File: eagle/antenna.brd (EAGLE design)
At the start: 120.7 x 57.1 mm, 23 parts

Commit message: cleaner antenna layout
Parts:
- C15: value 68 -> 86
- Q1: value (none) -> BUF730F
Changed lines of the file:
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@@
 </autorouter>
 <elements>
-<element name="Q1" library="transistor-small-signal" library_urn="urn:adsk.eagle:library:401" package="SOT343R" value="" x="14.605" y="29.21" smashed="yes" rot="R90">
-<attribute name="VALUE" x="17.305" y="28.11" size="1.27" layer="27" rot="R90"/>
-</element>
+<element name="Q1" library="transistor-small-signal" library_urn="urn:adsk.eagle:library:401" package="SOT343R" value="BUF730F" x="14.605" y="29.21" smashed="yes" rot="R90"/>
 <element name="L3" library="ref-packages-longpad" library_urn="urn:adsk.eagle:library:337" package="R0402" value="" x="12.065" y="30.48" smashed="yes" rot="R90">
 <attribute name="VALUE" x="13.97" y="29.845" size="1.27" layer="27" rot="R90"/>
@@
 <attribute name="VALUE" x="2.54" y="40.605" size="0.0254" layer="27"/>
 </element>
-<element name="C15" library="ref-packages-longpad" library_urn="urn:adsk.eagle:library:337" package="R0402" value="68" x="17.78" y="27.305" smashed="yes" rot="R180"/>
+<element name="C15" library="ref-packages-longpad" library_urn="urn:adsk.eagle:library:337" package="R0402" value="86" x="17.78" y="27.305" smashed="yes" rot="R180"/>
 </elements>
 <signals>

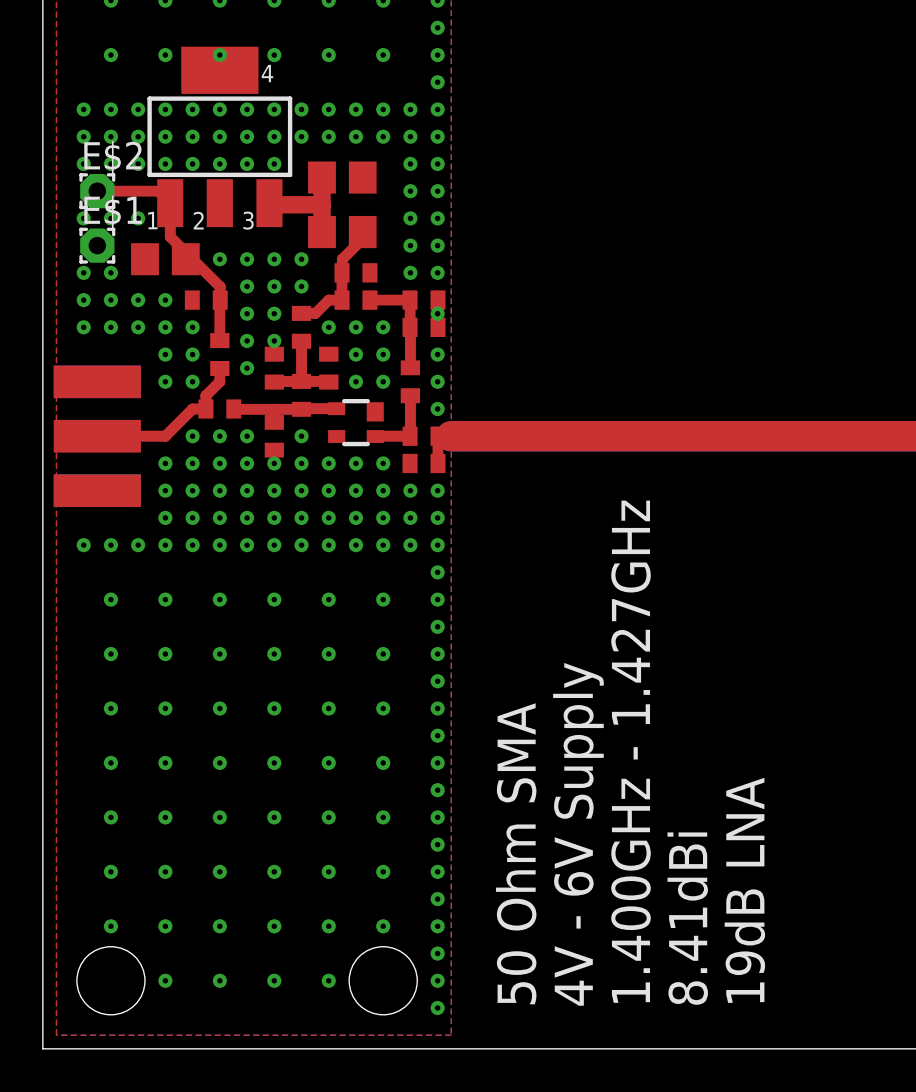
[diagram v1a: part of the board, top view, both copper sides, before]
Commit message: adjust LNA component values
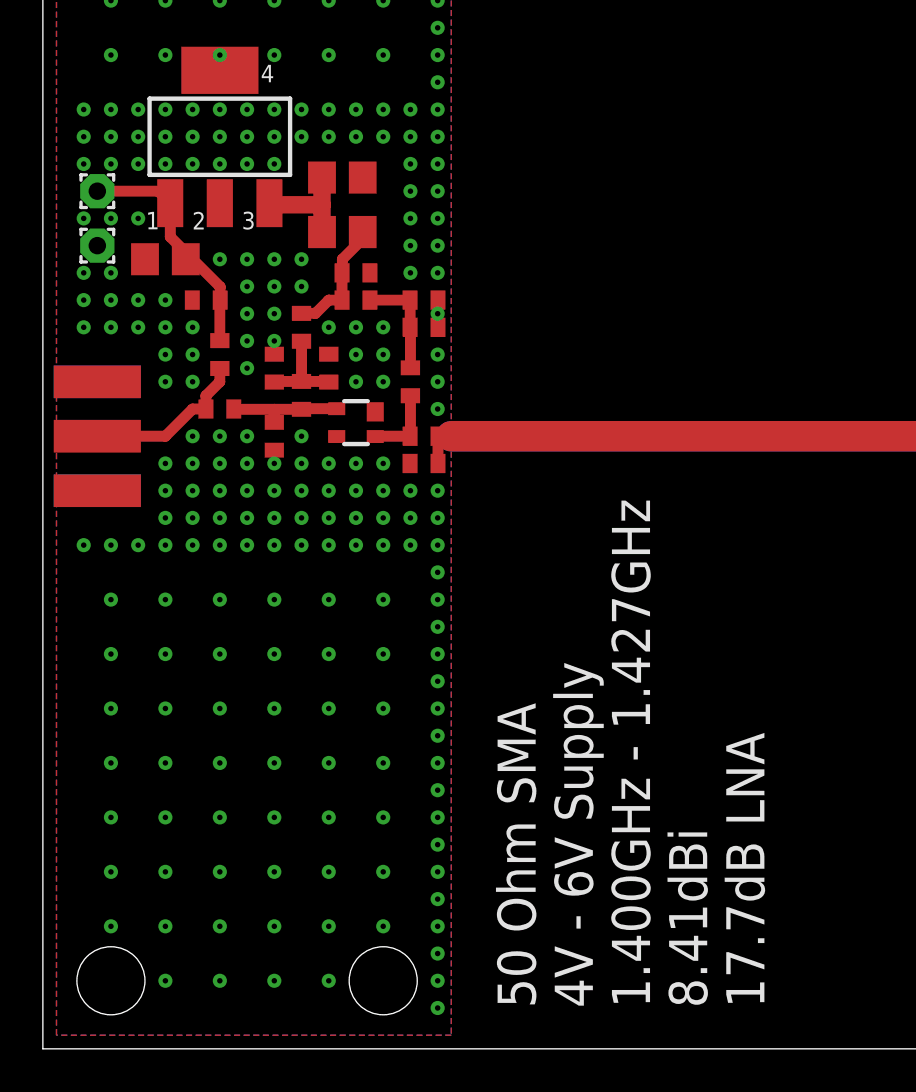
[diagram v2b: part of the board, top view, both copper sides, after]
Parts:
- C10, C3, C6, C9: value 1n -> 100p
- C5: value (none) -> 11p
- L3: value (none) -> 1.1n
- renumbered C14 to C10, C15 to R3, L5 to R2
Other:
- board text added: "50 Ohm SMA 4V - 6V Supply 1.400GHz - 1.427GHz 8.41dBi 17.7dB LNA"
- board text removed: "50 Ohm SMA 4V - 6V Supply 1.400GHz - 1.427GHz 8.41dBi 19dB LNA"
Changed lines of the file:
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@@
 1.400GHz - 1.427GHz
 8.41dBi
-19dB LNA</text>
+17.7dB LNA</text>
 </plain>
 <attributes>
@@
 <elements>
 <element name="Q1" library="transistor-small-signal" library_urn="urn:adsk.eagle:library:401" package="SOT343R" value="BUF730F" x="14.605" y="29.21" smashed="yes" rot="R90"/>
-<element name="L3" library="ref-packages-longpad" library_urn="urn:adsk.eagle:library:337" package="R0402" value="" x="12.065" y="30.48" smashed="yes" rot="R90">
-<attribute name="VALUE" x="13.97" y="29.845" size="1.27" layer="27" rot="R90"/>
-</element>
+<element name="L3" library="ref-packages-longpad" library_urn="urn:adsk.eagle:library:337" package="R0402" value="1.1n" x="12.065" y="30.48" smashed="yes" rot="R90"/>
 <element name="L2" library="ref-packages-longpad" library_urn="urn:adsk.eagle:library:337" package="R0402" value="22n" x="17.145" y="31.115" smashed="yes" rot="R90"/>
-<element name="C6" library="ref-packages-longpad" library_urn="urn:adsk.eagle:library:337" package="R0402" value="1n" x="17.78" y="33.655" smashed="yes"/>
+<element name="C6" library="ref-packages-longpad" library_urn="urn:adsk.eagle:library:337" package="R0402" value="100p" x="17.78" y="33.655" smashed="yes"/>
 <element name="C7" library="ref-packages-longpad" library_urn="urn:adsk.eagle:library:337" package="R0402" value="10n" x="17.78" y="34.925" smashed="yes"/>
 <element name="C8" library="ref-packages-longpad" library_urn="urn:adsk.eagle:library:337" package="R0402" value="10n" x="13.335" y="31.75" smashed="yes" rot="R90"/>
-<element name="C9" library="ref-packages-longpad" library_urn="urn:adsk.eagle:library:337" package="R0402" value="1n" x="10.795" y="31.75" smashed="yes" rot="R90"/>
-<element name="L5" library="ref-packages-longpad" library_urn="urn:adsk.eagle:library:337" package="R0402" value="51k" x="14.605" y="34.925" smashed="yes" rot="R180"/>
+<element name="C9" library="ref-packages-longpad" library_urn="urn:adsk.eagle:library:337" package="R0402" value="100p" x="10.795" y="31.75" smashed="yes" rot="R90"/>
+<element name="R2" library="ref-packages-longpad" library_urn="urn:adsk.eagle:library:337" package="R0402" value="51k" x="14.605" y="34.925" smashed="yes" rot="R180"/>
 <element name="E$11" library="SparkFun-Retired" library_urn="urn:adsk.eagle:library:533" package="SMA-EDGE" value="" x="2.54" y="26.035" smashed="yes" rot="R90"/>
 <element name="U1" library="transistor" library_urn="urn:adsk.eagle:library:402" package="SOT223" value="" x="8.255" y="42.545" smashed="yes">
@@
 <element name="L4" library="ref-packages-longpad" library_urn="urn:adsk.eagle:library:337" package="R0402" value="22n" x="12.065" y="33.655" smashed="yes" rot="R270"/>
 <element name="R1" library="rcl" library_urn="urn:adsk.eagle:library:334" package="R0805" package3d_urn="urn:adsk.eagle:package:23553/2" value="220" x="13.97" y="38.1" smashed="yes" rot="R180"/>
-<element name="C3" library="ref-packages-longpad" library_urn="urn:adsk.eagle:library:337" package="R0402" value="1n" x="8.255" y="29.845" smashed="yes" rot="R180"/>
+<element name="C3" library="ref-packages-longpad" library_urn="urn:adsk.eagle:library:337" package="R0402" value="100p" x="8.255" y="29.845" smashed="yes" rot="R180"/>
 <element name="L1" library="ref-packages-longpad" library_urn="urn:adsk.eagle:library:337" package="R0402" value="22n" x="8.255" y="32.385" smashed="yes" rot="R270"/>
 <element name="C4" library="ref-packages-longpad" library_urn="urn:adsk.eagle:library:337" package="R0402" value="10n" x="7.62" y="34.925" smashed="yes" rot="R180"/>
 <element name="C1" library="rcl" library_urn="urn:adsk.eagle:library:334" package="R0805" package3d_urn="urn:adsk.eagle:package:23553/2" value="1u" x="5.715" y="36.83" smashed="yes" rot="R180"/>
-<element name="C14" library="ref-packages-longpad" library_urn="urn:adsk.eagle:library:337" package="R0402" value="1n" x="17.78" y="28.575" smashed="yes" rot="R180"/>
-<element name="C5" library="ref-packages-longpad" library_urn="urn:adsk.eagle:library:337" package="R0402" value="" x="10.795" y="28.575" smashed="yes" rot="R270">
-<attribute name="VALUE" x="8.89" y="29.21" size="1.27" layer="27" rot="R270"/>
-</element>
+<element name="C10" library="ref-packages-longpad" library_urn="urn:adsk.eagle:library:337" package="R0402" value="100p" x="17.78" y="28.575" smashed="yes" rot="R180"/>
+<element name="C5" library="ref-packages-longpad" library_urn="urn:adsk.eagle:library:337" package="R0402" value="11p" x="10.795" y="28.575" smashed="yes" rot="R270"/>
 <element name="E$1" library="wirepad" library_urn="urn:adsk.eagle:library:412" package="1,6/0,8" package3d_urn="urn:adsk.eagle:package:30830/1" value="" x="2.54" y="37.465" smashed="yes">
-<attribute name="NAME" x="1.778" y="38.481" size="1.27" layer="25" ratio="10"/>
 <attribute name="VALUE" x="2.54" y="38.065" size="0.0254" layer="27"/>
 </element>
 <element name="E$2" library="wirepad" library_urn="urn:adsk.eagle:library:412" package="1,6/0,8" package3d_urn="urn:adsk.eagle:package:30830/1" value="" x="2.54" y="40.005" smashed="yes">
-<attribute name="NAME" x="1.778" y="41.021" size="1.27" layer="25" ratio="10"/>
 <attribute name="VALUE" x="2.54" y="40.605" size="0.0254" layer="27"/>
 </element>
-<element name="C15" library="ref-packages-longpad" library_urn="urn:adsk.eagle:library:337" package="R0402" value="86" x="17.78" y="27.305" smashed="yes" rot="R180"/>
+<element name="R3" library="ref-packages-longpad" library_urn="urn:adsk.eagle:library:337" package="R0402" value="86" x="17.78" y="27.305" smashed="yes" rot="R180"/>
 </elements>
 <signals>
@@
 <contactref element="E$1" pad="1"/>
 <via x="8.255" y="36.83" extent="1-16" drill="0.254"/>
-<contactref element="C15" pad="2"/>
+<contactref element="R3" pad="2"/>
 <via x="18.415" y="34.29" extent="1-16" drill="0.254"/>
 <via x="17.145" y="37.465" extent="1-16" drill="0.254"/>
@@
 <contactref element="L2" pad="1"/>
 <contactref element="Q1" pad="2"/>
-<contactref element="C14" pad="2"/>
+<contactref element="C10" pad="2"/>
 <wire x1="15.505" y1="28.56" x2="15.52" y2="28.575" width="0.508" layer="1"/>
 <wire x1="15.52" y1="28.575" x2="17.13" y2="28.575" width="0.508" layer="1"/>
@@
 <wire x1="104.013" y1="28.575" x2="104.013" y2="45.974" width="0.5588" layer="1"/>
 <wire x1="115.824" y1="28.575" x2="115.824" y2="12.7" width="0.508" layer="1"/>
-<contactref element="C14" pad="1"/>
+<contactref element="C10" pad="1"/>
 <wire x1="19.05" y1="28.575" x2="44.196" y2="28.575" width="1.4224" layer="1"/>
 <wire x1="18.43" y1="28.575" x2="19.05" y2="28.575" width="0.508" layer="1"/>
-<contactref element="C15" pad="1"/>
+<contactref element="R3" pad="1"/>
 <wire x1="18.43" y1="27.305" x2="18.43" y2="28.575" width="0.508" layer="1"/>
 </signal>
@@
 <contactref element="C6" pad="1"/>
 <contactref element="C7" pad="1"/>
-<contactref element="L5" pad="1"/>
+<contactref element="R2" pad="1"/>
 <contactref element="L2" pad="2"/>
 <wire x1="17.145" y1="31.765" x2="17.145" y2="33.64" width="0.508" layer="1"/>
@@
 </signal>
 <signal name="BIAS">
-<contactref element="L5" pad="2"/>
+<contactref element="R2" pad="2"/>
 <contactref element="L4" pad="1"/>
 <contactref element="C11" pad="1"/>

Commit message: more accurate spice sim of antenna LNA
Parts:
- C5: value 11p -> 12p
- C6, C9: value 100p -> 1n
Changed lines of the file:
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@@
 <element name="L3" library="ref-packages-longpad" library_urn="urn:adsk.eagle:library:337" package="R0402" value="1.1n" x="12.065" y="30.48" smashed="yes" rot="R90"/>
 <element name="L2" library="ref-packages-longpad" library_urn="urn:adsk.eagle:library:337" package="R0402" value="22n" x="17.145" y="31.115" smashed="yes" rot="R90"/>
-<element name="C6" library="ref-packages-longpad" library_urn="urn:adsk.eagle:library:337" package="R0402" value="100p" x="17.78" y="33.655" smashed="yes"/>
+<element name="C6" library="ref-packages-longpad" library_urn="urn:adsk.eagle:library:337" package="R0402" value="1n" x="17.78" y="33.655" smashed="yes"/>
 <element name="C7" library="ref-packages-longpad" library_urn="urn:adsk.eagle:library:337" package="R0402" value="10n" x="17.78" y="34.925" smashed="yes"/>
 <element name="C8" library="ref-packages-longpad" library_urn="urn:adsk.eagle:library:337" package="R0402" value="10n" x="13.335" y="31.75" smashed="yes" rot="R90"/>
-<element name="C9" library="ref-packages-longpad" library_urn="urn:adsk.eagle:library:337" package="R0402" value="100p" x="10.795" y="31.75" smashed="yes" rot="R90"/>
+<element name="C9" library="ref-packages-longpad" library_urn="urn:adsk.eagle:library:337" package="R0402" value="1n" x="10.795" y="31.75" smashed="yes" rot="R90"/>
 <element name="R2" library="ref-packages-longpad" library_urn="urn:adsk.eagle:library:337" package="R0402" value="51k" x="14.605" y="34.925" smashed="yes" rot="R180"/>
 <element name="E$11" library="SparkFun-Retired" library_urn="urn:adsk.eagle:library:533" package="SMA-EDGE" value="" x="2.54" y="26.035" smashed="yes" rot="R90"/>
@@
 <element name="C1" library="rcl" library_urn="urn:adsk.eagle:library:334" package="R0805" package3d_urn="urn:adsk.eagle:package:23553/2" value="1u" x="5.715" y="36.83" smashed="yes" rot="R180"/>
 <element name="C10" library="ref-packages-longpad" library_urn="urn:adsk.eagle:library:337" package="R0402" value="100p" x="17.78" y="28.575" smashed="yes" rot="R180"/>
-<element name="C5" library="ref-packages-longpad" library_urn="urn:adsk.eagle:library:337" package="R0402" value="11p" x="10.795" y="28.575" smashed="yes" rot="R270"/>
+<element name="C5" library="ref-packages-longpad" library_urn="urn:adsk.eagle:library:337" package="R0402" value="12p" x="10.795" y="28.575" smashed="yes" rot="R270"/>
 <element name="E$1" library="wirepad" library_urn="urn:adsk.eagle:library:412" package="1,6/0,8" package3d_urn="urn:adsk.eagle:package:30830/1" value="" x="2.54" y="37.465" smashed="yes">
 <attribute name="VALUE" x="2.54" y="38.065" size="0.0254" layer="27"/>

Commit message: marginally better antenna match
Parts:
- R3: value 86 -> 91
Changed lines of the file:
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@@
 <attribute name="VALUE" x="2.54" y="40.605" size="0.0254" layer="27"/>
 </element>
-<element name="R3" library="ref-packages-longpad" library_urn="urn:adsk.eagle:library:337" package="R0402" value="86" x="17.78" y="27.305" smashed="yes" rot="R180"/>
+<element name="R3" library="ref-packages-longpad" library_urn="urn:adsk.eagle:library:337" package="R0402" value="91" x="17.78" y="27.305" smashed="yes" rot="R180"/>
 </elements>
 <signals>
